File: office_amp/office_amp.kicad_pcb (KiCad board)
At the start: 4 copper layers, 120 x 100 mm, 140 parts, among them J1 Jack-DC, J2 Conn_01x03_Female, J3 Conn_02x07_Odd_Even, J7 Screw_Terminal_01x04, J8 Conn_01x03_Female, K1 EC2-24NU, K2 EC2-24NU, K3 EC2-24NU, K4 EC2-24NU, Q1 DMT6012LSS, Q2 BC858, Q3 BC858, Q4 BC850, Q5 BC850, Q6 BC856, Q7 BC850, Q8 BC856, Q9 BC856, U1 LM74700, U10 DS1882E, U12 TL082, U2 TBA_2-2421, U3 TL082, U4 TBA_2-2421, U5 MH-M18, U6 TPA3123D2, U7 TL082, U8 IL300, U9 IL300

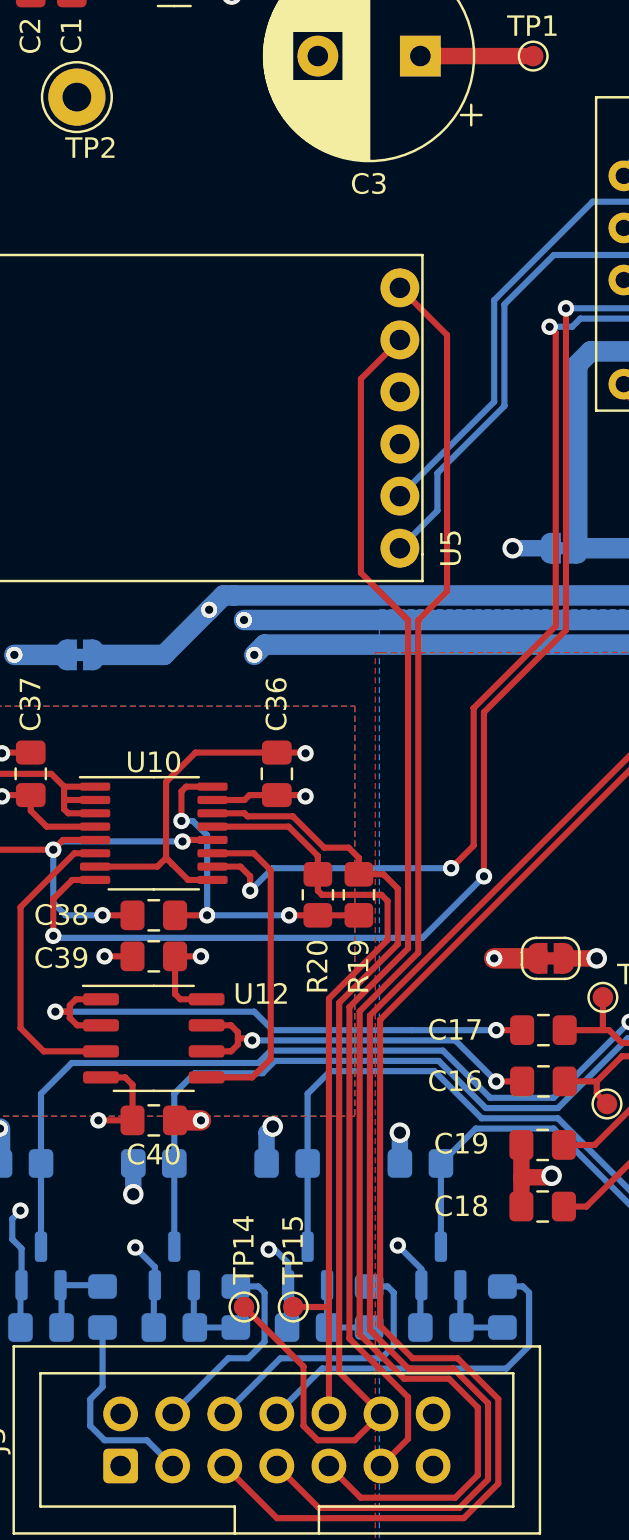
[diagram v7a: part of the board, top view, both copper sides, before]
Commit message: Added bluetooth vcc filter, moved i2c pullups to controll board, added touch controller
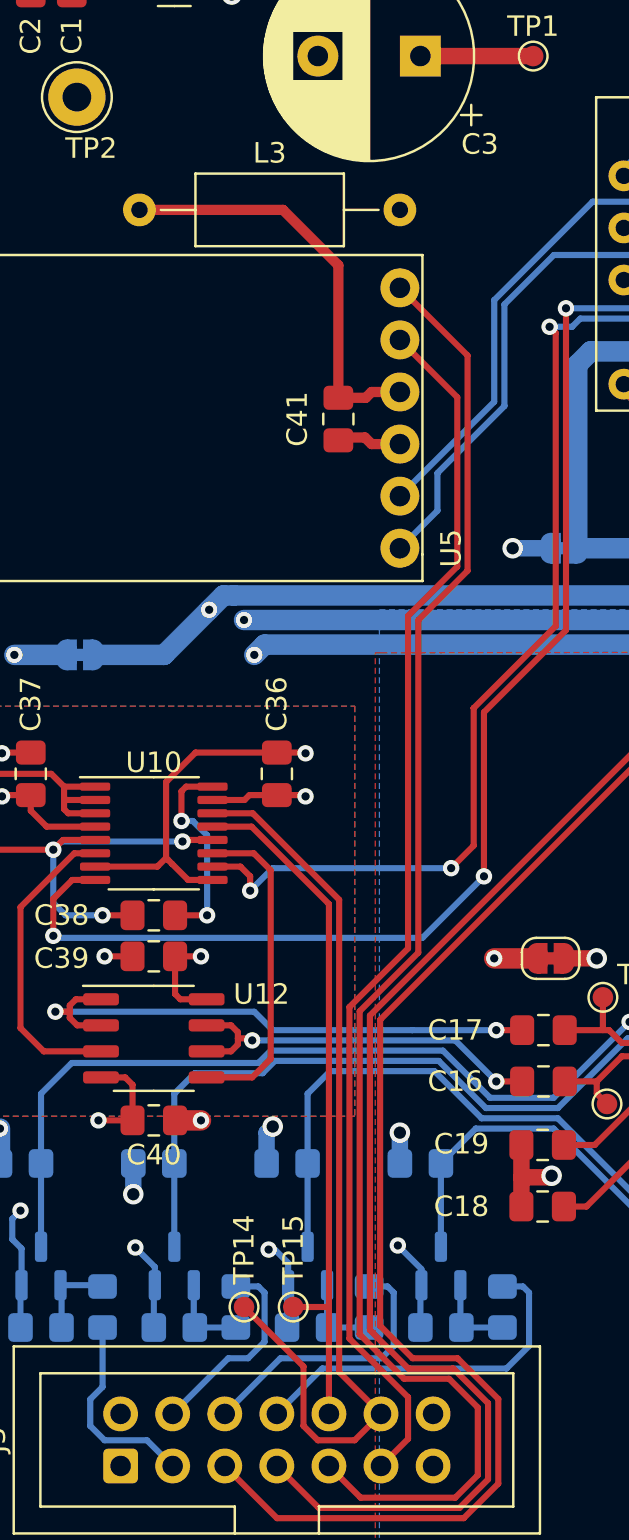
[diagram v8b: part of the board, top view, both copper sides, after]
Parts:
- removed R19, R20: 4k7, Resistor_SMD:R_0805_2012Metric_Pad1.20x1.40mm_HandSolder
- added C41: 10µF, Capacitor_SMD:C_0805_2012Metric_Pad1.18x1.45mm_HandSolder, F.Cu at (110.0, 99.7)
- added L3: 100µH, Inductor_THT:L_Axial_L7.0mm_D3.3mm_P12.70mm_Horizontal_Fastron_MICC, F.Cu at (100.3, 89.5)
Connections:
- U5 pad 4: 5V_BT -> Net-(C41-Pad1)
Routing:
- net Net-(C41-Pad1): track 0.00 -> 20.4 mm
- net +3V3: track 116.5 -> 109.1 mm, vias 7 -> 6
- net SDA: track 38.8 -> 33.7 mm
- net SCL: track 50.3 -> 45.4 mm
- net GND_BT: track 18.9 -> 22.1 mm
- net BT-KEY: track 72.6 -> 73.5 mm
- net 5V_BT: track 20.2 -> 20.8 mm
